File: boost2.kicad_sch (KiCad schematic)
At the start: 26 parts, among them Q6 BSC059N04LS6, Q7 BSC059N04LS6, U1 TPS43061

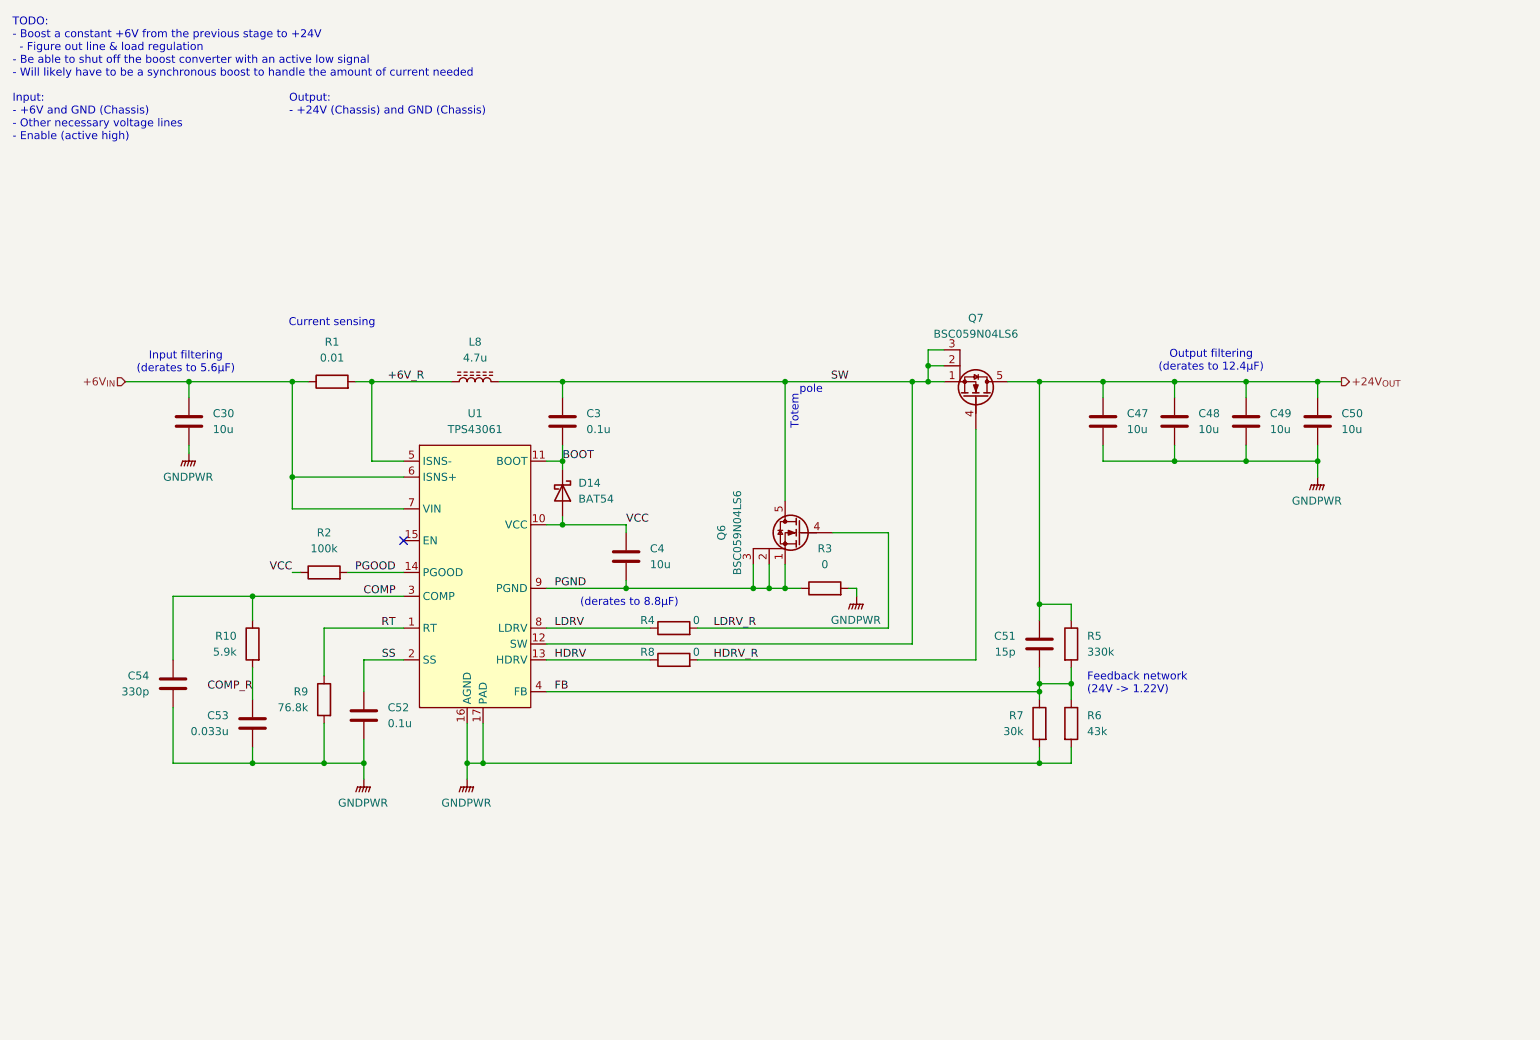
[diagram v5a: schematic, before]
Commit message: Made 2nd stage boost functional
Next possible steps: make 1st stage be able to handle even more current because the sims did not explode while supplying 3A of current (!)
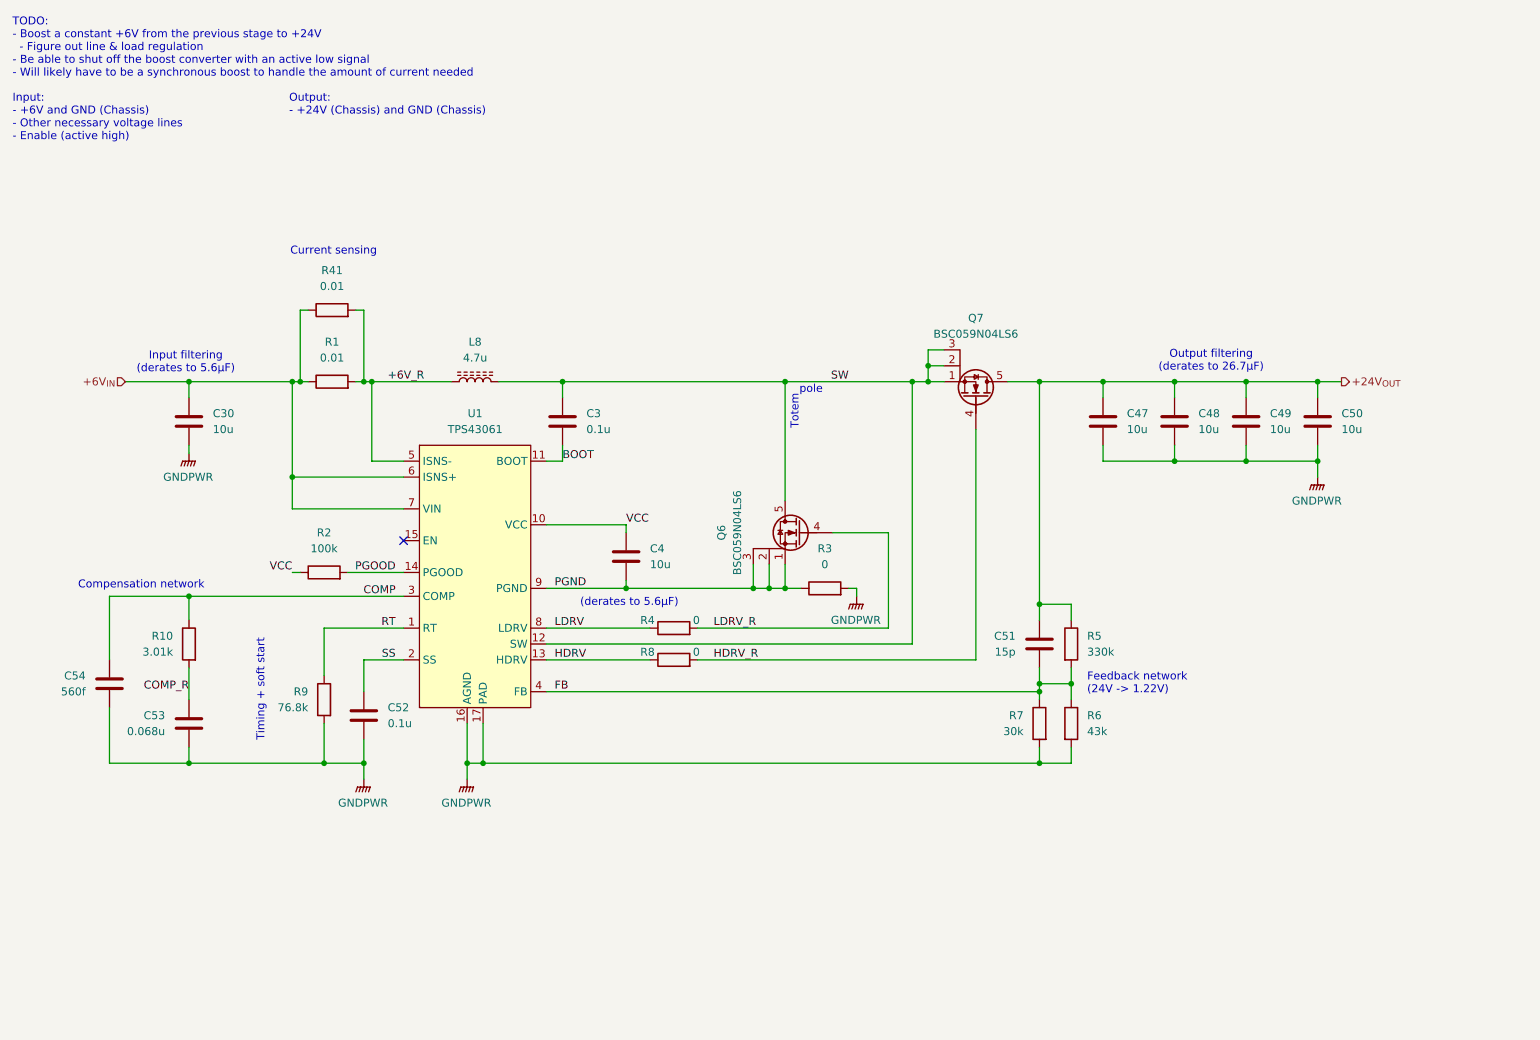
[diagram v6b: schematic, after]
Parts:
- removed D14: BAT54, Package_TO_SOT_SMD:SOT-23_Handsoldering, symbol Device:D_Schottky
- added R41: 0.01, Resistor_SMD:R_0612_1632Metric_Pad1.18x3.40mm_HandSolder, symbol Device:R
- C53: value 0.033u -> 0.068u
- C54: value 330p -> 560f; Mouser Part Number (none) -> 603-CC603BRNPO9BNR56
- R10: value 5.9k -> 3.01k
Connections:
- net +6V_R: now also R41.2
- net +6V_{IN}: now also R41.1
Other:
- note added: "(derates to 5.6µF)"
- note added: "Compensation network"
- note added: "Output filtering (derates to 26.7µF)"
- note added: "Timing + soft start"
- note removed: "(derates to 8.8µF)"
- note removed: "Output filtering (derates to 12.4µF)"
- moved on the sheet: C53, C54, R10

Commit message: Considering using a different IC for 1st stage
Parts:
- C53: value 0.068u -> 0.1u
- C54: value 560f -> 1000p; Mouser Part Number 603-CC603BRNPO9BNR56 -> (none)
- R10: value 3.01k -> 2.49k
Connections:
- net +6V_{IN} renamed +5.5V_{IN}
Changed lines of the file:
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@@
 		)
 	)
-	(hierarchical_label "+6V_{IN}"
+	(hierarchical_label "+5.5V_{IN}"
 		(shape input)
 		(at 41.91 78.74 180)
@@
 			)
 		)
-		(property "Value" "3.01k"
+		(property "Value" "2.49k"
 			(at 49.53 121.9199 0)
 			(effects
@@
 			)
 		)
-		(property "Value" "0.068u"
+		(property "Value" "0.1u"
 			(at 48.26 134.6199 0)
 			(effects
@@
 			)
 		)
-		(property "Value" "560f"
+		(property "Value" "1000p"
 			(at 35.56 128.2699 0)
 			(effects
@@
 			)
 		)
-		(property "Mouser Part Number" "603-CC603BRNPO9BNR56"
+		(property "Mouser Part Number" ""
 			(at 39.37 127 0)
 			(effects

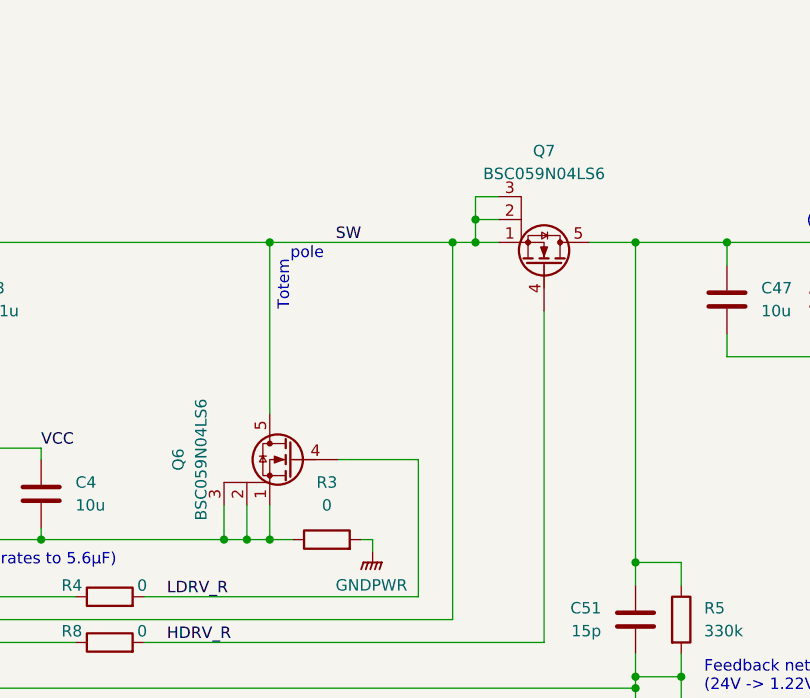
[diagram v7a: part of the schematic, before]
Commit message: Redesigning output boosts to be more efficient albeit with less current capacity
idk what I changed with the schematics lol
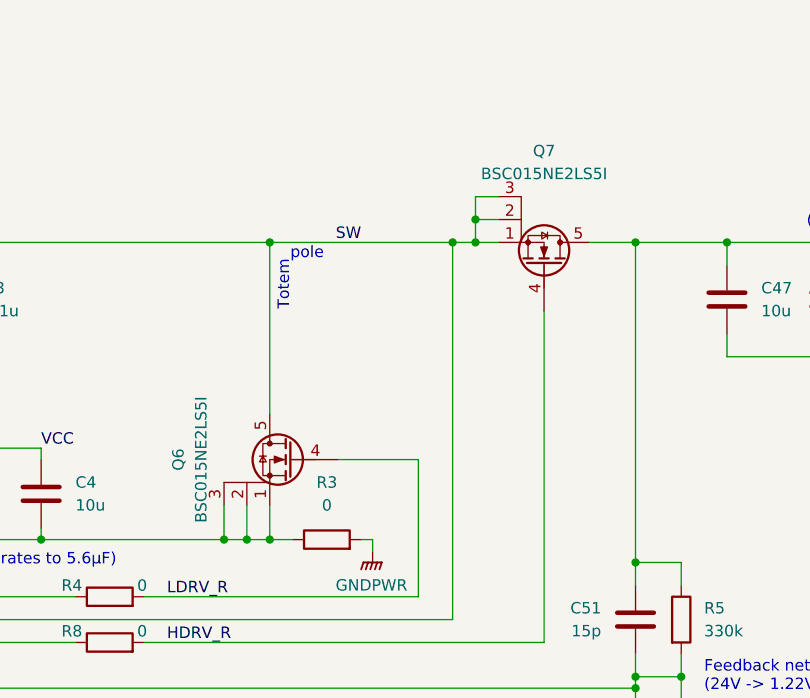
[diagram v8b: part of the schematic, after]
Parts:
- Q6, Q7: value BSC059N04LS6 -> BSC015NE2LS5I; Mouser Part Number 726-BSC059N04LS6ATMA -> 726-BSC015NE2LS5IATM
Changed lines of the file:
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@@
 			)
 		)
-		(property "Value" "BSC059N04LS6"
+		(property "Value" "BSC015NE2LS5I"
 			(at 139.7 102.87 90)
 			(effects
@@
 			)
 		)
-		(property "Datasheet" "https://www.mouser.com/datasheet/2/196/Infineon_BSC059N04LS6_DataSheet_v02_01_EN-3360636.pdf"
+		(property "Datasheet" "https://www.mouser.com/datasheet/2/196/Infineon_BSC015NE2LS5I_DataSheet_v02_01_EN-3360635.pdf"
 			(at 149.86 102.87 0)
 			(effects
@@
 			)
 		)
-		(property "Mouser Part Number" "726-BSC059N04LS6ATMA"
+		(property "Mouser Part Number" "726-BSC015NE2LS5IATM"
 			(at 149.86 102.87 0)
 			(effects
@@
 			)
 		)
-		(property "Value" "BSC059N04LS6"
+		(property "Value" "BSC015NE2LS5I"
 			(at 177.8 71.12 90)
 			(effects
@@
 			)
 		)
-		(property "Datasheet" "https://www.mouser.com/datasheet/2/196/Infineon_BSC059N04LS6_DataSheet_v02_01_EN-3360636.pdf"
+		(property "Datasheet" "https://www.mouser.com/datasheet/2/196/Infineon_BSC015NE2LS5I_DataSheet_v02_01_EN-3360635.pdf"
 			(at 177.8 81.28 0)
 			(effects
@@
 			)
 		)
-		(property "Mouser Part Number" "726-BSC059N04LS6ATMA"
+		(property "Mouser Part Number" "726-BSC015NE2LS5IATM"
 			(at 177.8 81.28 0)
 			(effects
